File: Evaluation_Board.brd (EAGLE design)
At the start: 60.9 x 39.4 mm, 38 parts, among them IC1 MEGA32-A, IC2 FT232RL, IC3 317EMP, J1 DCJ0202, Q1 16 MHz

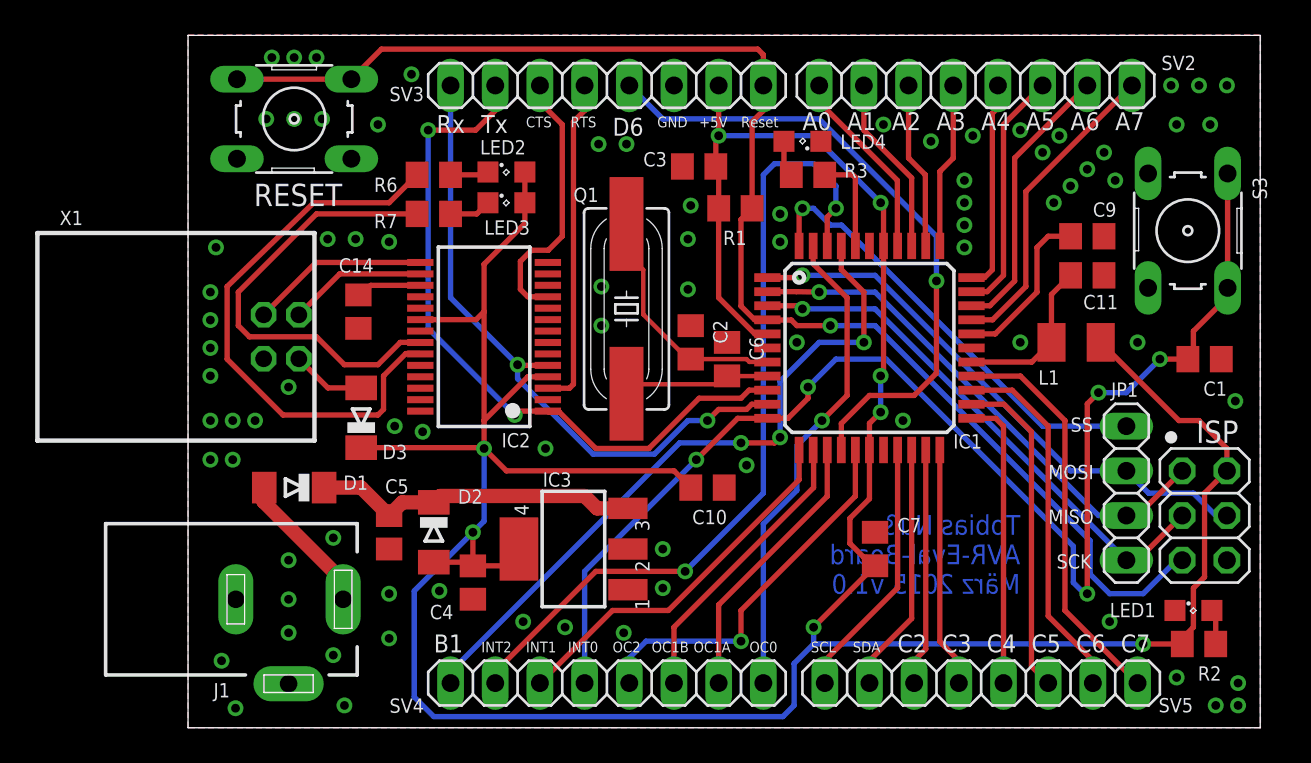
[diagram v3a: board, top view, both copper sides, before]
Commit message: Few changes. Placed two wires new to get better ground plane.
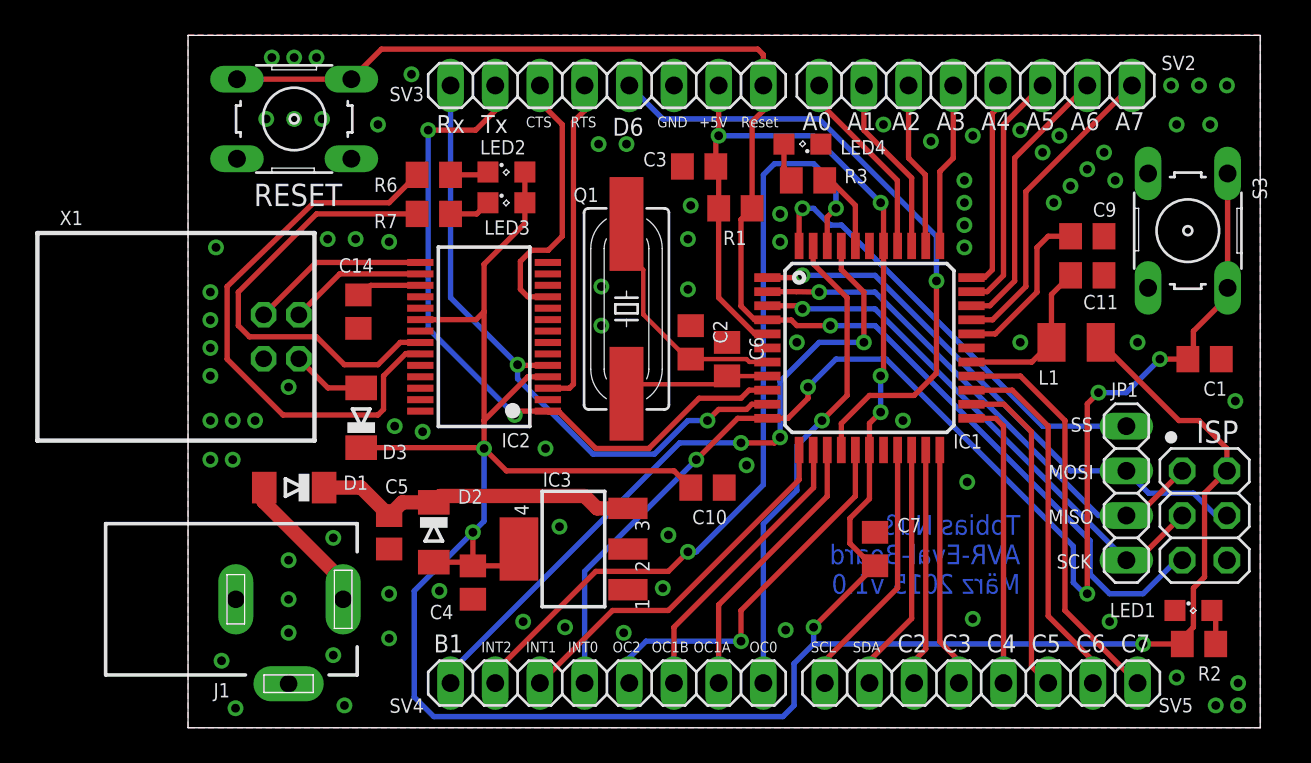
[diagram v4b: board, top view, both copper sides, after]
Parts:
- moved R3 0.32 mm to (35.2, 31.1)
- moved LED4 0.16 mm to (34.9, 33.2)
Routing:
- net PB0: track 5.70 -> 4.59 mm
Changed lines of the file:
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@@
 <?xml version="1.0" encoding="utf-8"?>
 <!DOCTYPE eagle SYSTEM "eagle.dtd">
-<eagle version="6.4">
+<eagle version="6.5.0">
 <drawing>
 <settings>
@@
 <layer number="45" name="Holes" color="7" fill="1" visible="no" active="yes"/>
 <layer number="46" name="Milling" color="3" fill="1" visible="no" active="yes"/>
-<layer number="47" name="Measures" color="7" fill="1" visible="no" active="yes"/>
+<layer number="47" name="Measures" color="7" fill="1" visible="yes" active="yes"/>
 <layer number="48" name="Document" color="7" fill="1" visible="no" active="yes"/>
 <layer number="49" name="Reference" color="7" fill="1" visible="no" active="yes"/>
@@
 <attribute name="VALUE" x="51.7525" y="31.3055" size="1.27" layer="27" ratio="10" rot="R270"/>
 </element>
-<element name="LED4" library="led" package="SML0805" value="yellow" x="34.925" y="33.3375" smashed="yes" rot="R180">
-<attribute name="NAME" x="37.07625" y="32.90875" size="0.8128" layer="25"/>
-<attribute name="VALUE" x="36.425" y="35.3375" size="1.27" layer="27" rot="R180"/>
-</element>
-<element name="R3" library="rcl" package="R0805" value="500" x="35.2425" y="31.4325" smashed="yes">
-<attribute name="NAME" x="37.30625" y="31.27375" size="0.8128" layer="25"/>
-<attribute name="VALUE" x="34.6075" y="28.8925" size="1.27" layer="27"/>
+<element name="LED4" library="led" package="SML0805" value="yellow" x="34.925" y="33.17875" smashed="yes" rot="R180">
+<attribute name="NAME" x="37.07625" y="32.59125" size="0.8128" layer="25"/>
+<attribute name="VALUE" x="36.425" y="35.17875" size="1.27" layer="27" rot="R180"/>
+</element>
+<element name="R3" library="rcl" package="R0805" value="500" x="35.2425" y="31.115" smashed="yes">
+<attribute name="NAME" x="37.30625" y="30.95625" size="0.8128" layer="25"/>
+<attribute name="VALUE" x="34.6075" y="28.575" size="1.27" layer="27"/>
 </element>
 <element name="JP1" library="pinhead" package="1X04" value="" x="53.34" y="13.335" smashed="yes" rot="R90">
@@
 <via x="19.05" y="6.0325" extent="1-16" drill="0.5"/>
 <via x="26.9875" y="7.9375" extent="1-16" drill="0.5"/>
-<via x="26.9875" y="10.16" extent="1-16" drill="0.5"/>
+<via x="27.305" y="10.95375" extent="1-16" drill="0.5"/>
 <via x="33.655" y="29.21" extent="1-16" drill="0.5"/>
 <via x="44.60875" y="33.655" extent="1-16" drill="0.5"/>
@@
 <contactref element="J1" pad="2"/>
 <contactref element="J1" pad="3"/>
+<via x="21.11375" y="11.43" extent="1-16" drill="0.5"/>
+<via x="44.29125" y="13.97" extent="1-16" drill="0.5"/>
+<via x="33.9725" y="5.55625" extent="1-16" drill="0.5"/>
+<via x="44.60875" y="6.19125" extent="1-16" drill="0.5"/>
 </signal>
 <signal name="+5V">
@@
 <wire x1="17.4625" y1="2.54" x2="17.4625" y2="3.175" width="0.3048" layer="1"/>
 <wire x1="17.4625" y1="3.175" x2="23.1775" y2="8.89" width="0.3048" layer="1"/>
-<wire x1="23.1775" y1="8.89" x2="28.2575" y2="8.89" width="0.3048" layer="1"/>
+<wire x1="23.1775" y1="8.89" x2="27.305" y2="8.89" width="0.3048" layer="1"/>
 <wire x1="36.335" y1="27.39" x2="36.335" y2="29.0325" width="0.3048" layer="1"/>
 <wire x1="36.335" y1="29.0325" x2="36.83" y2="29.5275" width="0.3048" layer="1"/>
@@
 <wire x1="36.83" y1="29.5275" x2="36.83" y2="30.7975" width="0.3048" layer="16"/>
 <wire x1="36.83" y1="30.7975" x2="35.56" y2="32.0675" width="0.3048" layer="16"/>
-<wire x1="32.7025" y1="31.4325" x2="32.7025" y2="13.335" width="0.3048" layer="16"/>
-<via x="28.2575" y="8.89" extent="1-16" drill="0.5"/>
+<wire x1="32.7025" y1="31.4325" x2="32.7025" y2="13.81125" width="0.3048" layer="16"/>
 <wire x1="32.7025" y1="31.4325" x2="33.3375" y2="32.0675" width="0.3048" layer="16"/>
 <wire x1="33.3375" y1="32.0675" x2="35.56" y2="32.0675" width="0.3048" layer="16"/>
-<wire x1="28.2575" y1="8.89" x2="32.7025" y2="13.335" width="0.3048" layer="16"/>
+<wire x1="27.305" y1="8.89" x2="28.41625" y2="10.00125" width="0.3048" layer="1"/>
+<via x="28.41625" y="10.00125" extent="1-16" drill="0.5"/>
+<wire x1="28.41625" y1="10.00125" x2="28.8925" y2="10.00125" width="0.3048" layer="16"/>
+<wire x1="28.8925" y1="10.00125" x2="32.7025" y2="13.81125" width="0.3048" layer="16"/>
 </signal>
 <signal name="PD3_INT1">
@@
 <contactref element="R3" pad="2"/>
 <contactref element="IC1" pad="40"/>
-<wire x1="37.935" y1="27.39" x2="37.935" y2="31.28" width="0.3048" layer="1"/>
-<wire x1="37.935" y1="31.28" x2="37.7825" y2="31.4325" width="0.3048" layer="1"/>
-<wire x1="37.7825" y1="31.4325" x2="36.1925" y2="31.4325" width="0.3048" layer="1"/>
+<wire x1="37.935" y1="27.39" x2="37.935" y2="29.6925" width="0.3048" layer="1"/>
+<wire x1="37.935" y1="29.6925" x2="36.67125" y2="30.95625" width="0.3048" layer="1"/>
+<wire x1="36.67125" y1="30.95625" x2="36.1925" y2="31.115" width="0.3048" layer="1"/>
 </signal>
 <signal name="N$26">
 <contactref element="R3" pad="1"/>
 <contactref element="LED4" pad="A"/>
-<wire x1="34.2925" y1="31.4325" x2="33.875" y2="31.85" width="0.3048" layer="1"/>
-<wire x1="33.875" y1="31.85" x2="33.875" y2="33.3375" width="0.3048" layer="1"/>
+<wire x1="34.2925" y1="31.115" x2="33.875" y2="31.85" width="0.3048" layer="1"/>
+<wire x1="33.875" y1="31.85" x2="33.875" y2="33.17875" width="0.3048" layer="1"/>
 </signal>
 <signal name="PB1">
